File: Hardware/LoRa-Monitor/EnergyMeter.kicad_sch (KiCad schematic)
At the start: 76 parts, among them U14 ATM90E32AS-AU-R, U16 ADuM1401xRW, U17 ADuM1401xRW, U18 ADuM1401xRW, X1 16.384MHz

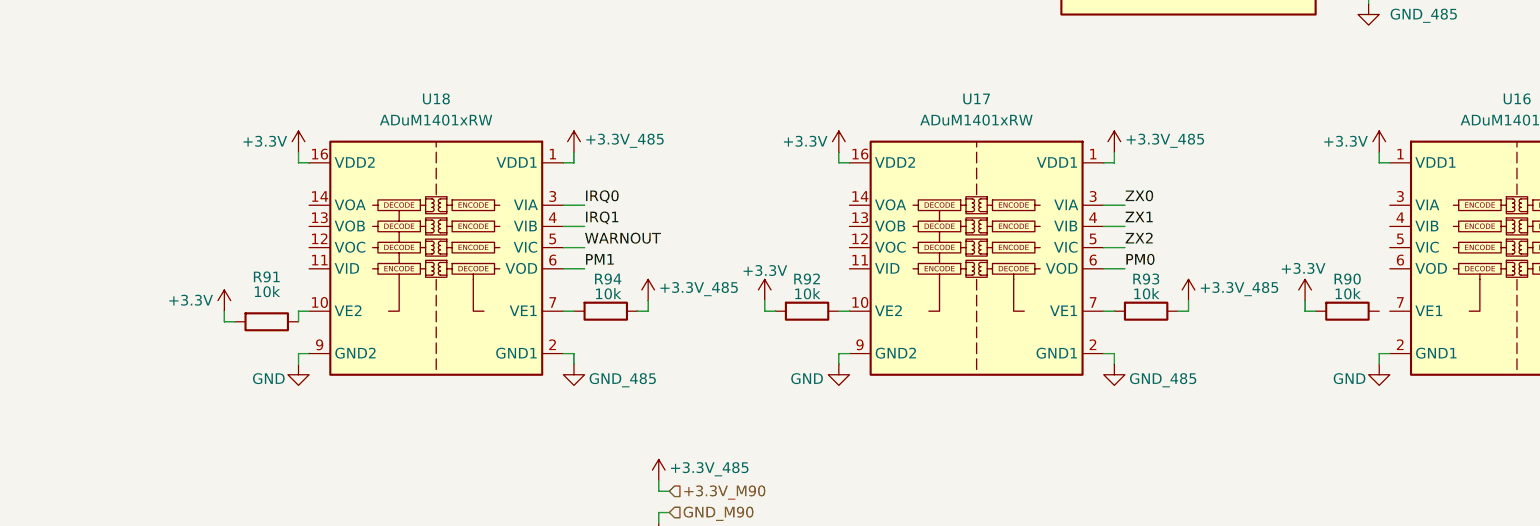
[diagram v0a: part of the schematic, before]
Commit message: Finished Energy Meter Module, started LoRa Module and MCU.
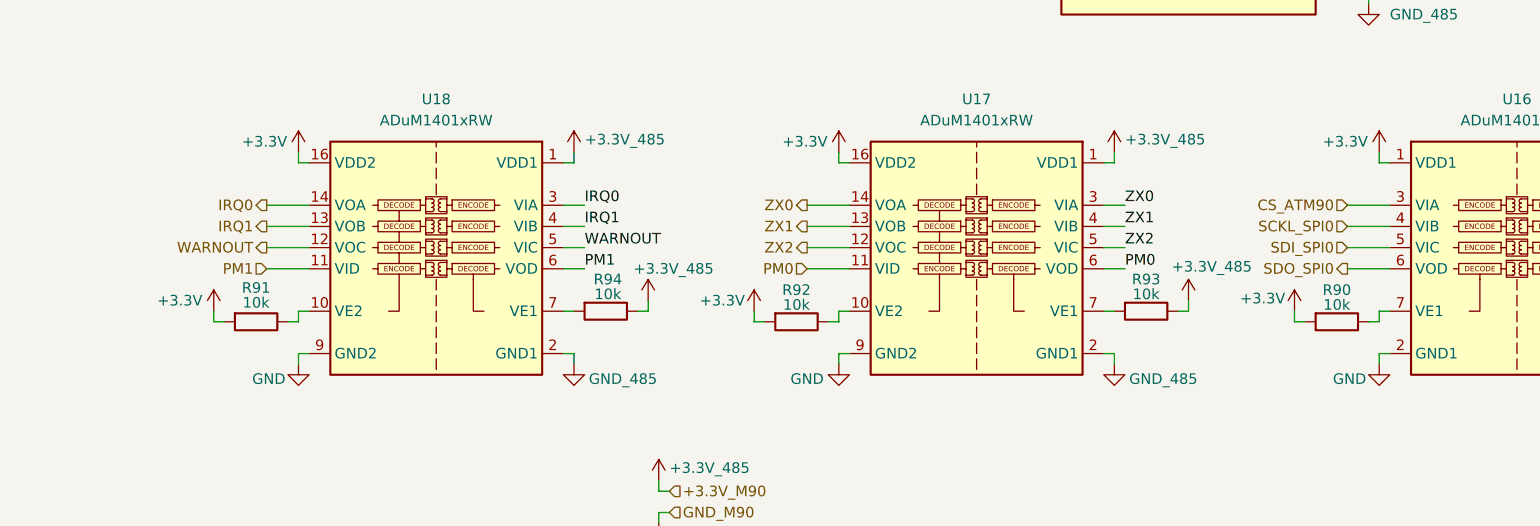
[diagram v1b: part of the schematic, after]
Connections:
- net IRQ0: now also U18.14 (VOA)
- net IRQ1: now also U18.13 (VOB)
- net PM0: now also U17.11 (VID)
- net PM1: now also U18.11 (VID)
- net WARNOUT: now also U18.12 (VOC)
- net ZX0: now also U17.14 (VOA)
- net ZX1: now also U17.13 (VOB)
- net ZX2: now also U17.12 (VOC)
- net at R90.1: now also U16.7 (VE1)
- net CS_ATM90: now reaches U16.3 (VIA)
- net SCKL_SPI0: now reaches U16.4 (VIB)
- net SDI_SPI0: now reaches U16.5 (VIC)
- net SDO_SPI0: now reaches U16.6 (VOD)
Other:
- moved on the sheet: R90, R91, R92

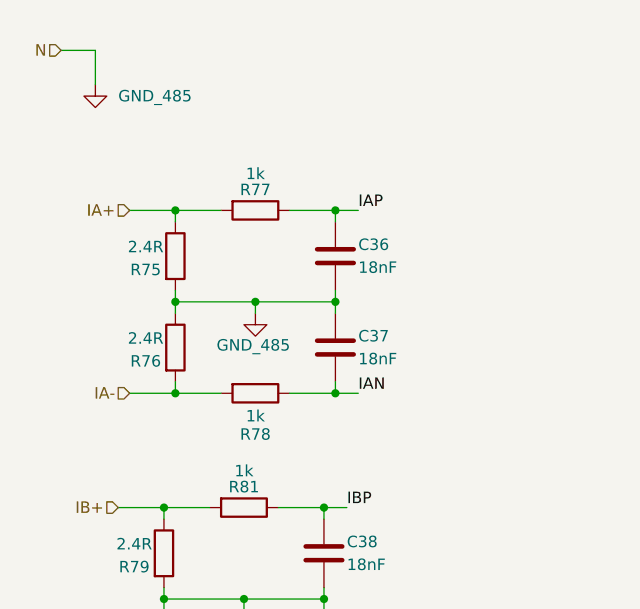
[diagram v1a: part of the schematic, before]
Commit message: Finished MCU and Lora modules. Finished Connectors sheet
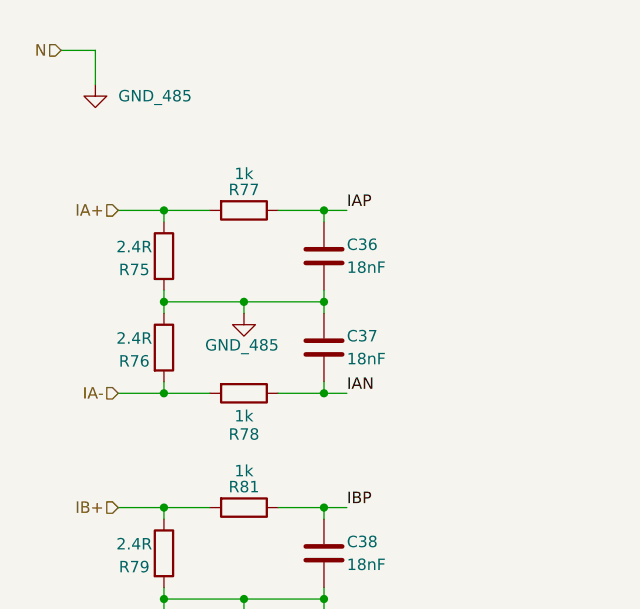
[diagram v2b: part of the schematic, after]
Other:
- moved on the sheet: C36, C37, R75, R76, R77, R78

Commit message: Finished schematic, started with PCB design
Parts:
- removed R45, R46, R47: 10k, Resistor_SMD:R_0805_2012Metric, symbol Device:R
- removed R48: 240k, Resistor_SMD:R_0805_2012Metric, symbol Device:R
- added R111, R112, R113: 10k, Resistor_SMD:R_0805_2012Metric, symbol Device:R
- added R114: 240k, Resistor_SMD:R_0805_2012Metric, symbol Device:R
- C23: value 4.7uF -> 10uF
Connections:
- net IRQ0: no longer U14.30 (IRQ0), U18.3 (VIA)
- net IRQ1: no longer U14.31 (IRQ1), U18.4 (VIB)
- net PM0: no longer R88.2, U14.33 (PM0), U17.6 (VOD)
- net PM1: no longer R87.2, U14.34 (PM1), U18.6 (VOD)
- net SCKL: now also R111.2
- net SDI: now also R112.2
- net SDO: now also R113.2
- net Ua: now also R114.2
- net WARNOUT: no longer U14.29 (WARNOUT), U18.5 (VIC)
- net ZX0: no longer U14.22 (ZX0), U17.3 (VIA)
- net ZX1: no longer U14.23 (ZX1), U17.4 (VIB)
- net ZX2: no longer U14.24 (ZX2), U17.5 (VIC)
- net at R49.2: now also R114.1
- net +3.3V_485 renamed +3.3V_M90
- net +3.3V_M90: now also R111.1, R112.1, R113.1
- new net: U14.35 (NC), U14.45 (NC), U14.46 (NC)
- new net IRQ0_M90: U14.30 (IRQ0), U18.3 (VIA)
- new net IRQ1_M90: U14.31 (IRQ1), U18.4 (VIB)
- new net PM0_M90: R88.2, U14.33 (PM0), U17.6 (VOD)
- new net PM1_M90: R87.2, U14.34 (PM1), U18.6 (VOD)
- new net WARNOUT_M90: U14.29 (WARNOUT), U18.5 (VIC)
- new net ZX0_M90: U14.22 (ZX0), U17.3 (VIA)
- new net ZX1_M90: U14.23 (ZX1), U17.4 (VIB)
- new net ZX2_M90: U14.24 (ZX2), U17.5 (VIC)
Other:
- moved on the sheet: C23, C24, C25, C26, C28, C29, R89, R90, U16

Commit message: Started routing.
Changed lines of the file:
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@@
 	(symbol
 		(lib_id "power:+3.3V")
+		(at 250.19 33.02 0)
+		(unit 1)
+		(body_style 1)
+		(exclude_from_sim no)
+		(in_bom yes)
+		(on_board yes)
+		(in_pos_files yes)
+		(dnp no)
+		(property "Reference" "#PWR096"
+			(at 250.19 36.83 0)
+			(hide yes)
+			(show_name no)
+			(do_not_autoplace no)
+			(effects
+				(font
+					(size 1.27 1.27)
+				)
+			)
+		)
+		(property "Value" "+3.3V_M90"
+			(at 256.286 31.496 0)
+			(show_name no)
+			(do_not_autoplace no)
+			(effects
+				(font
+					(size 1.27 1.27)
+				)
+			)
+		)
+		(property "Footprint" ""
+			(at 250.19 33.02 0)
+			(hide yes)
+			(show_name no)
+			(do_not_autoplace no)
+			(effects
+				(font
+					(size 1.27 1.27)
+				)
+			)
+		)
+		(property "Datasheet" ""
+			(at 250.19 33.02 0)
+			(hide yes)
+			(show_name no)
+			(do_not_autoplace no)
+			(effects
+				(font
+					(size 1.27 1.27)
+				)
+			)
+		)
+		(property "Description" "Power symbol creates a global label with name \"+3.3V\""
+			(at 250.19 33.02 0)
+			(hide yes)
+			(show_name no)
+			(do_not_autoplace no)
+			(effects
+				(font
+					(size 1.27 1.27)
+				)
+			)
+		)
+		(pin "1"
+		)
+		(instances
+			(project "LoRa-Monitor"
+				(path "/7510cc7d-c141-46d4-8947-7def3af8cf35/d3ce2e9b-3d29-41cf-a745-789309f3e1db"
+					(reference "#PWR096")
+					(unit 1)
+				)
+			)
+		)
+	)
+	(symbol
+		(lib_id "power:+3.3V")
 		(at 274.32 149.86 0)
 		(unit 1)
@@
 	)
 	(symbol
-		(lib_id "power:+3.3V")
-		(at 250.19 33.02 0)
-		(unit 1)
-		(body_style 1)
-		(exclude_from_sim no)
-		(in_bom yes)
-		(on_board yes)
-		(in_pos_files yes)
-		(dnp no)
-		(property "Reference" "#PWR078"
-			(at 250.19 36.83 0)
-			(hide yes)
-			(show_name no)
-			(do_not_autoplace no)
-			(effects
-				(font
-					(size 1.27 1.27)
-				)
-			)
-		)
-		(property "Value" "+3.3V_M90"
-			(at 256.286 31.496 0)
-			(show_name no)
-			(do_not_autoplace no)
-			(effects
-				(font
-					(size 1.27 1.27)
-				)
-			)
-		)
-		(property "Footprint" ""
-			(at 250.19 33.02 0)
-			(hide yes)
-			(show_name no)
-			(do_not_autoplace no)
-			(effects
-				(font
-					(size 1.27 1.27)
-				)
-			)
-		)
-		(property "Datasheet" ""
-			(at 250.19 33.02 0)
-			(hide yes)
-			(show_name no)
-			(do_not_autoplace no)
-			(effects
-				(font
-					(size 1.27 1.27)
-				)
-			)
-		)
-		(property "Description" "Power symbol creates a global label with name \"+3.3V\""
-			(at 250.19 33.02 0)
-			(hide yes)
-			(show_name no)
-			(do_not_autoplace no)
-			(effects
-				(font
-					(size 1.27 1.27)
-				)
-			)
-		)
-		(pin "1"
-		)
-		(instances
-			(project "LoRa-Monitor"
-				(path "/7510cc7d-c141-46d4-8947-7def3af8cf35/d3ce2e9b-3d29-41cf-a745-789309f3e1db"
-					(reference "#PWR078")
-					(unit 1)
-				)
-			)
-		)
-	)
-	(symbol
 		(lib_id "Device:R")
 		(at 35.56 66.04 270)
@@
 					(unit 1)
 				)
+			)
+		)
+	)
+	(symbol
+		(lib_id "power:PWR_FLAG")
+		(at 250.19 36.83 270)
+		(unit 1)
+		(body_style 1)
+		(exclude_from_sim no)
+		(in_bom yes)
+		(on_board yes)
+		(in_pos_files yes)
+		(dnp no)
+		(fields_autoplaced yes)
+		(property "Reference" "#FLG04"
+			(at 252.095 36.83 0)
+			(hide yes)
+			(show_name no)
+			(do_not_autoplace no)
+			(effects
+				(font
+					(size 1.27 1.27)
+				)
+			)
+		)
+		(property "Value" "PWR_FLAG"
+			(at 254 36.8299 90)
+			(show_name no)
+			(do_not_autoplace no)
+			(effects
+				(font
+					(size 1.27 1.27)
+				)
+				(justify left)
+			)
+		)
+		(property "Footprint" ""
+			(at 250.19 36.83 0)
+			(hide yes)
+			(show_name no)
+			(do_not_autoplace no)
+			(effects
+				(font
+					(size 1.27 1.27)
+				)
+			)
+		)
+		(property "Datasheet" ""
+			(at 250.19 36.83 0)
+			(hide yes)
+			(show_name no)
+			(do_not_autoplace no)
+			(effects
+				(font
+					(size 1.27 1.27)
+				)
+			)
+		)
+		(property "Description" "Special symbol for telling ERC where power comes from"
+			(at 250.19 36.83 0)
+			(hide yes)
+			(show_name no)
+			(do_not_autoplace no)
+			(effects
+				(font
+					(size 1.27 1.27)
+				)
+			)
+		)
+		(pin "1"
+		)
+		(instances
+			(project "LoRa-Monitor"
+				(path "/7510cc7d-c141-46d4-8947-7def3af8cf35/d3ce2e9b-3d29-41cf-a745-789309f3e1db"
+					(reference "#FLG04")
+					(unit 1)
+				)

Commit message: Finished the first component disposition
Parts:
- R114, R49, R50, R51, R52, R53, R54, R57, R58, R59, R60, R61, R62, R63, R66, R67, R68, R69, R70, R71, R72: footprint Resistor_SMD:R_0805_2012Metric -> Resistor_SMD:R_1206_3216Metric
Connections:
- net IRQ0: now also U18.11 (VID); no longer U18.14 (VOA)
- net IRQ0_M90: now also U18.6 (VOD); no longer U18.3 (VIA)
- net IRQ1: now also U18.12 (VOC); no longer U18.13 (VOB)
- net IRQ1_M90: now also U18.5 (VIC); no longer U18.4 (VIB)
- net PM0: now also U18.13 (VOB); no longer U17.11 (VID)
- net PM0_M90: now also U18.4 (VIB); no longer U17.6 (VOD)
- net PM1: now also U18.14 (VOA); no longer U18.11 (VID)
- net PM1_M90: now also U18.3 (VIA); no longer U18.6 (VOD)
- net WARNOUT: now also U17.14 (VOA); no longer U18.12 (VOC)
- net WARNOUT_M90: now also U17.3 (VIA); no longer U18.5 (VIC)
- net ZX0: now also U17.11 (VID); no longer U17.14 (VOA)
- net ZX0_M90: now also U17.6 (VOD); no longer U17.3 (VIA)
- net ZX1: now also U17.12 (VOC); no longer U17.13 (VOB)
- net ZX1_M90: now also U17.5 (VIC); no longer U17.4 (VIB)
- net ZX2: now also U17.13 (VOB); no longer U17.12 (VOC)
- net ZX2_M90: now also U17.4 (VIB); no longer U17.5 (VIC)
